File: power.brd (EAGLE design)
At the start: 90.2 x 95.9 mm, 59 parts, among them J1 POWER_JACKPTH_BREAD, T1 SINGLE_NCHAN_FET, T2 SINGLE_NCHAN_FET, T3 SINGLE_NCHAN_FET, U1 MOSFET_PCHAN_20A, U14 MOSFET_PCHAN_20A, U2 MOSFET_PCHAN_20A

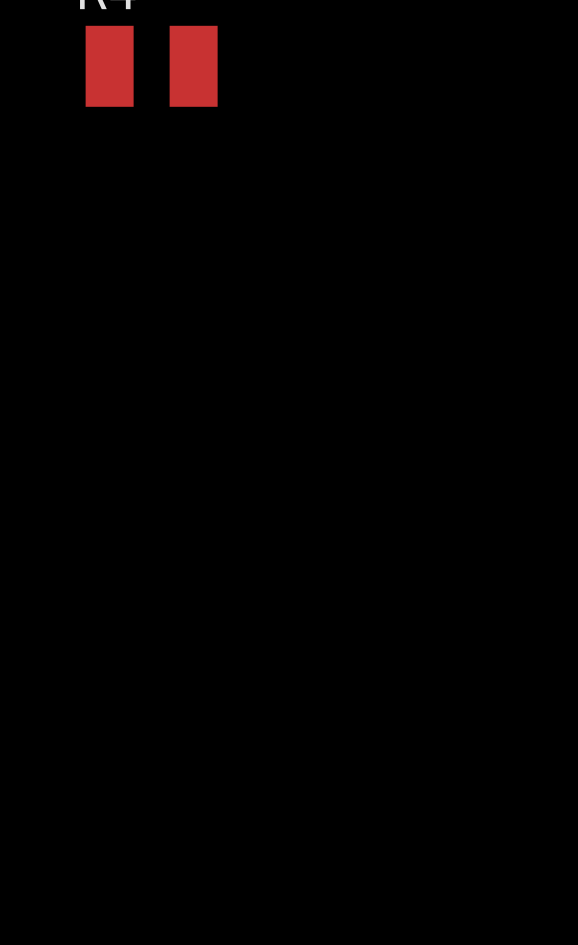
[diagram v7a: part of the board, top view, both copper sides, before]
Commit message: Added current sensors to power board
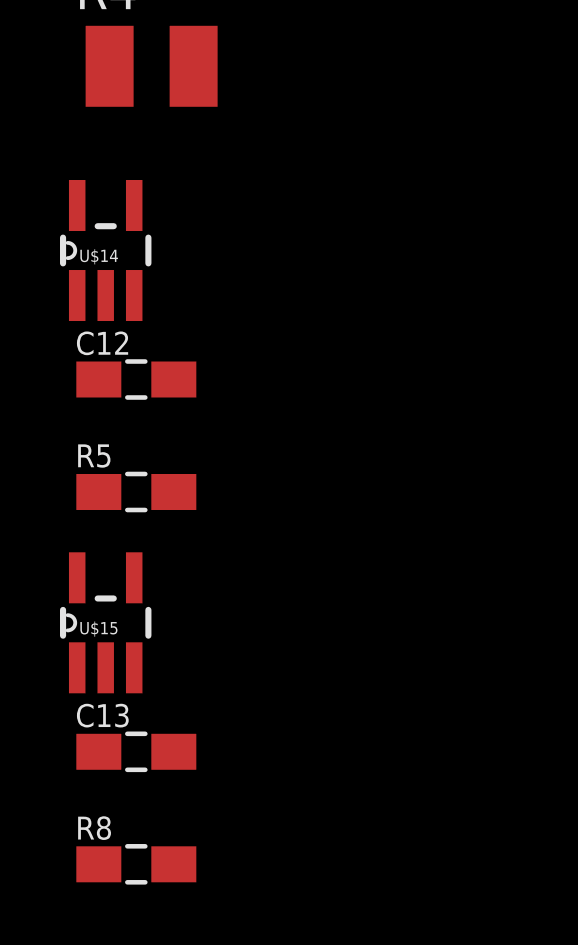
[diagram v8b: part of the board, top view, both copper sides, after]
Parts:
- added C12, C13: .1uF, phonesat:0805
- added R5, R8: .2R prec, phonesat:0805
- added U$14, U$15: CURRENT_MAX4372, phonesat:SOT23-5
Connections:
- new net I_BATT: U$15.2
- new net I_SOLAR: U$14.2
- new net VREG_IN: C1.1, H2.45, H2.46, JP5.1, R2.2, R27.2, R4.2, R6.2, R8.1, R9.2, U$13.VIN, U$15.5, U1.1, U1.2, U1.3, U14.1, U14.2, U14.3, U2.1, U2.2, U2.3
- net 3.3V: now also C12.1, C13.1, U$14.3, U$15.3
- net GND: now also C12.2, C13.2, U$14.1, U$15.1
- net VBATT: now also R5.1, R8.2, U$14.5, U$15.4; no longer C1.1, H2.45, H2.46, JP5.1, R2.2, R27.2, R4.2, R6.2, R9.2, U$13.VIN, U1.1, U1.2, U1.3, U14.1, U14.2, U14.3, U2.1, U2.2, U2.3
- net VSOLAR: now also R5.2, U$14.4
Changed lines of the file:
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@@
 <element name="R1" library="rcl" package="R1210" value="0R" x="-53.24" y="-145.74"/>
 <element name="R4" library="rcl" package="R1210" value="0R" x="-53.24" y="-150.85"/>
+<element name="U$14" library="phonesat" package="SOT23-5" value="CURRENT_MAX4372" x="-54.77" y="-156.99"/>
+<element name="R5" library="phonesat" package="0805" value=".2R prec" x="-53.75" y="-165.04"/>
+<element name="C12" library="phonesat" package="0805" value=".1uF" x="-53.75" y="-161.29"/>
+<element name="U$15" library="phonesat" package="SOT23-5" value="CURRENT_MAX4372" x="-54.77" y="-169.4"/>
+<element name="C13" library="phonesat" package="0805" value=".1uF" x="-53.75" y="-173.7"/>
+<element name="R8" library="phonesat" package="0805" value=".2R prec" x="-53.75" y="-177.45"/>
 </elements>
 <signals>
@@
 <contactref element="C10" pad="2"/>
 <contactref element="C11" pad="2"/>
+<contactref element="U$14" pad="1"/>
+<contactref element="C12" pad="2"/>
+<contactref element="U$15" pad="1"/>
+<contactref element="C13" pad="2"/>
+<wire x1="-52.5" y1="-173.7" x2="-55.72" y2="-170.9001" width="0" layer="19" extent="1-1"/>
+<wire x1="-52.5" y1="-161.29" x2="-55.72" y2="-170.9001" width="0" layer="19" extent="1-1"/>
+<wire x1="-55.72" y1="-158.4901" x2="-52.5" y2="-161.29" width="0" layer="19" extent="1-1"/>
+<wire x1="-53.87" y1="-124.81" x2="-55.72" y2="-158.4901" width="0" layer="19" extent="1-1"/>
 <wire x1="-50.92" y1="-124.81" x2="-53.87" y2="-124.81" width="0" layer="19" extent="1-1"/>
 <wire x1="-49.77" y1="-124.81" x2="-50.92" y2="-124.81" width="0" layer="19" extent="1-1"/>
@@
 <wire x1="64.77" y1="85.73" x2="7.07" y2="21.05" width="0" layer="19" extent="1-1"/>
 </signal>
-<signal name="VBATT">
+<signal name="VREG_IN">
 <contactref element="H2" pad="45"/>
 <contactref element="H2" pad="46"/>
@@
 <contactref element="JP5" pad="1"/>
 <contactref element="R4" pad="2"/>
+<contactref element="U$15" pad="5"/>
+<contactref element="R8" pad="1"/>
+<wire x1="-55.72" y1="-167.8999" x2="-55" y2="-177.45" width="0" layer="19" extent="1-1"/>
+<wire x1="-51.84" y1="-150.85" x2="-55.72" y2="-167.8999" width="0" layer="19" extent="1-1"/>
 <wire x1="-52.49" y1="-138.74" x2="-51.84" y2="-150.85" width="0" layer="19" extent="1-1"/>
 <wire x1="-3.47" y1="-124.81" x2="-52.49" y2="-138.74" width="0" layer="19" extent="1-1"/>
@@
 <contactref element="U$13" pad="BIAS"/>
 <contactref element="L2" pad="P2"/>
-<wire x1="-38.74" y1="-124.81" x2="32.585" y2="55.07" width="0" layer="19" extent="1-1"/>
+<contactref element="U$14" pad="3"/>
+<contactref element="C12" pad="1"/>
+<contactref element="U$15" pad="3"/>
+<contactref element="C13" pad="1"/>
+<wire x1="-53.82" y1="-170.9001" x2="-55" y2="-173.7" width="0" layer="19" extent="1-1"/>
+<wire x1="-55" y1="-161.29" x2="-53.82" y2="-170.9001" width="0" layer="19" extent="1-1"/>
+<wire x1="-53.82" y1="-158.4901" x2="-55" y2="-161.29" width="0" layer="19" extent="1-1"/>
+<wire x1="-38.74" y1="-124.81" x2="-53.82" y2="-158.4901" width="0" layer="19" extent="1-1"/>
 <wire x1="-22.97" y1="-124.81" x2="-38.74" y2="-124.81" width="0" layer="19" extent="1-1"/>
 <wire x1="-17.77" y1="-124.81" x2="-22.97" y2="-124.81" width="0" layer="19" extent="1-1"/>
-<wire x1="45.985" y1="55.665" x2="-17.77" y2="-124.81" width="0" layer="19" extent="1-1"/>
+<wire x1="32.585" y1="55.07" x2="-17.77" y2="-124.81" width="0" layer="19" extent="1-1"/>
+<wire x1="45.985" y1="55.665" x2="32.585" y2="55.07" width="0" layer="19" extent="1-1"/>
 <wire x1="46.99" y1="88.27" x2="45.985" y2="55.665" width="0" layer="19" extent="1-1"/>
 <wire x1="46.99" y1="90.81" x2="46.99" y2="88.27" width="0" layer="19" extent="1-1"/>
@@
 <contactref element="U$5" pad="P6"/>
 <contactref element="U$5" pad="P3"/>
-<wire x1="59.79" y1="42.47" x2="59.79" y2="43.72" width="0" layer="19" extent="1-1"/>
+<contactref element="U$14" pad="4"/>
+<contactref element="R5" pad="2"/>
+<wire x1="-53.82" y1="-155.4899" x2="-52.5" y2="-165.04" width="0" layer="19" extent="1-1"/>
+<wire x1="59.79" y1="42.47" x2="-53.82" y2="-155.4899" width="0" layer="19" extent="1-1"/>
+<wire x1="59.79" y1="43.72" x2="59.79" y2="42.47" width="0" layer="19" extent="1-1"/>
 </signal>
 <signal name="N$7">
@@
 <contactref element="R7" pad="1"/>
 </signal>
+<signal name="I_SOLAR">
+<contactref element="U$14" pad="2"/>
+</signal>
+<signal name="I_BATT">
+<contactref element="U$15" pad="2"/>
+</signal>
+<signal name="VBATT">
+<contactref element="U$15" pad="4"/>
+<contactref element="R8" pad="2"/>
+<contactref element="U$14" pad="5"/>
+<contactref element="R5" pad="1"/>
+<wire x1="-53.82" y1="-167.8999" x2="-52.5" y2="-177.45" width="0" layer="19" extent="1-1"/>
+<wire x1="-55" y1="-165.04" x2="-53.82" y2="-167.8999" width="0" layer="19" extent="1-1"/>
+<wire x1="-55.72" y1="-155.4899" x2="-55" y2="-165.04" width="0" layer="19" extent="1-1"/>
+</signal>
 </signals>
